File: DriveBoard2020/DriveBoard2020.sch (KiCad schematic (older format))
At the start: 78 parts, among them SW0 SW_SPST, SW1 SW_Push, SW2 SW_Push, SW3 SW_Push, SW4 SW_Push, SW5 SW_Push, SW6 SW_Push, SW7 SW_Push, SW8 SW_Push, SW9 SW_Push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

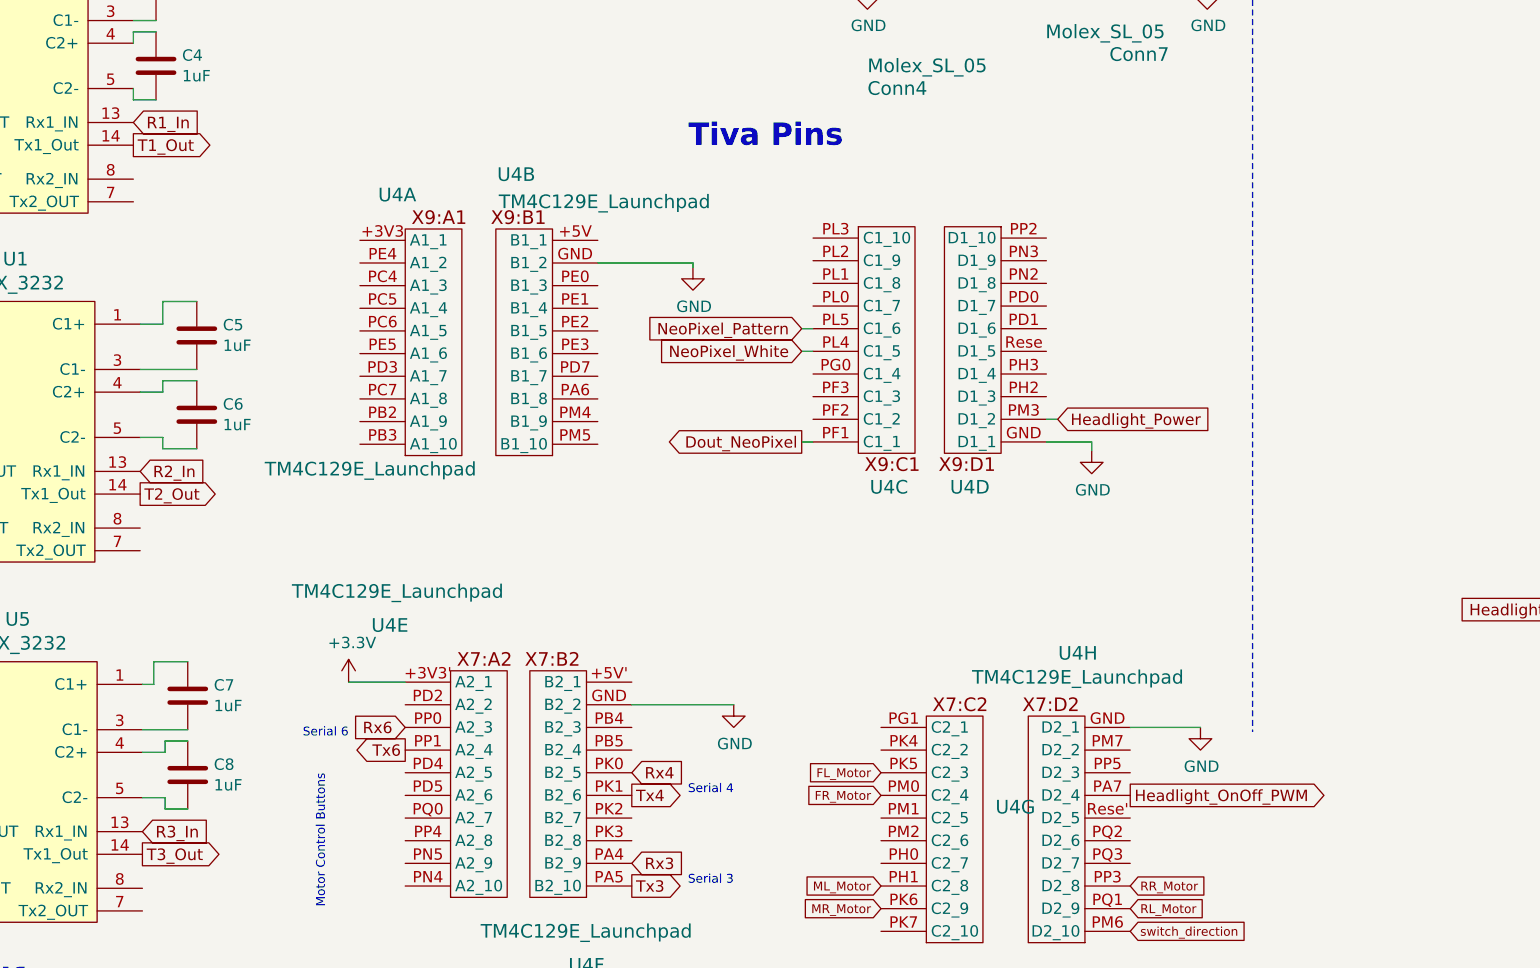
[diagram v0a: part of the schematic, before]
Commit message: finished placing components on layout
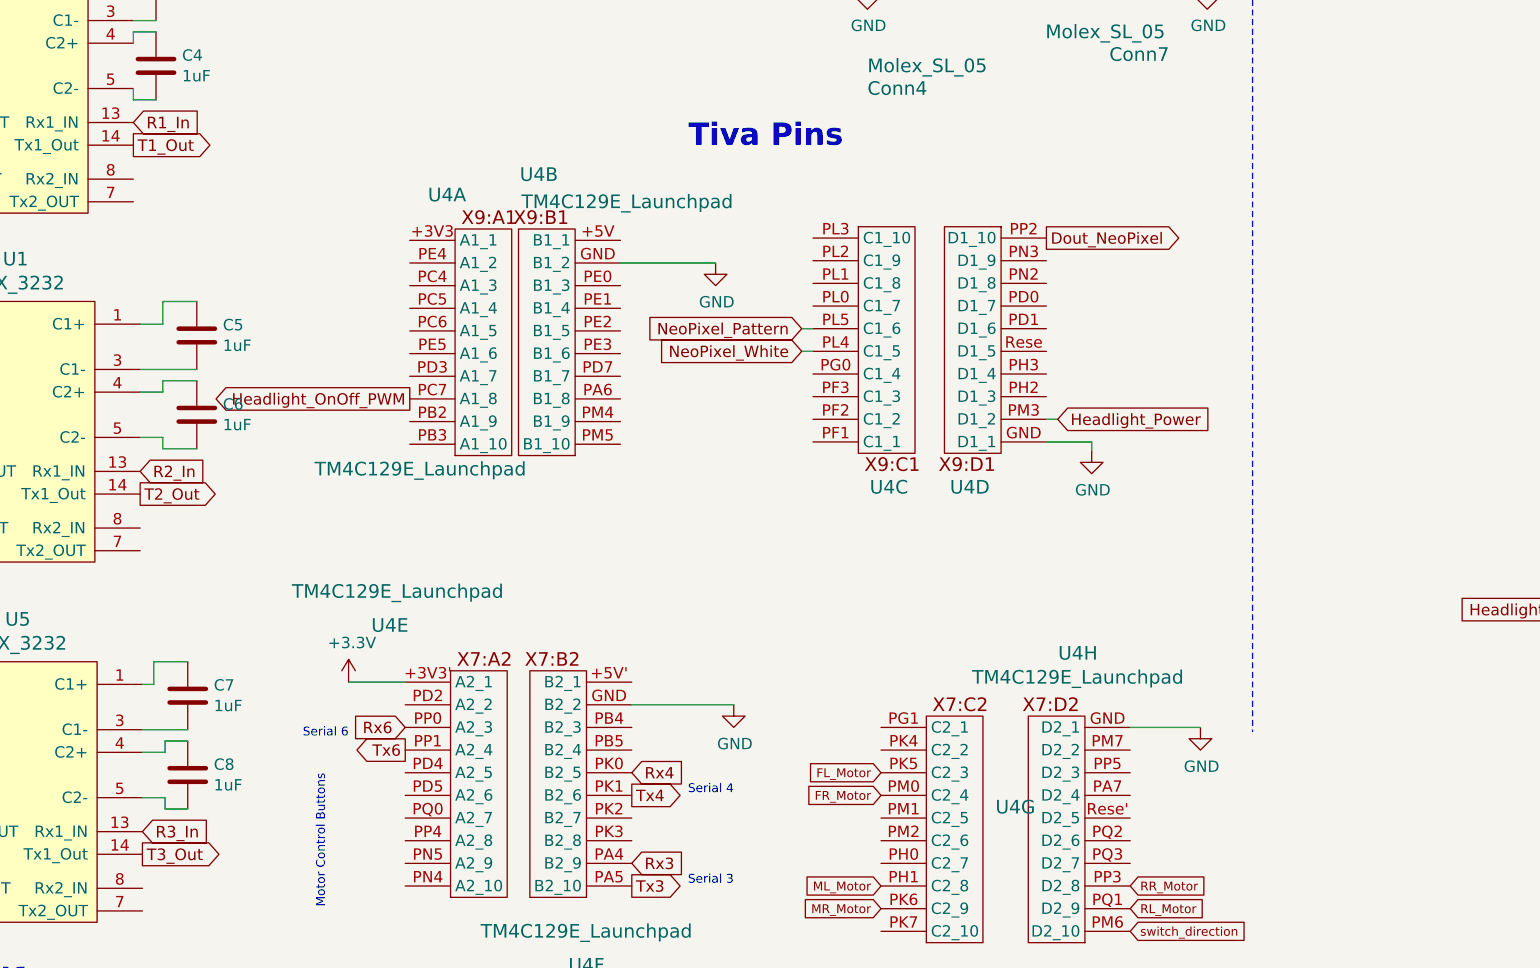
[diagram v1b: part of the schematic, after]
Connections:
- net Dout_NeoPixel: now also U4.PP2 (D1_10); no longer U4.PF1 (C1_1)
- net Headlight_OnOff_PWM: now also U4.PC7 (A1_8); no longer U4.PA7 (D2_4)
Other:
- moved on the sheet: U4A, U4B
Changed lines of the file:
@@
 	1    0    0    1
 $EndComp
-Text GLabel 4980 5260 0    50   Output ~ 0
+Text GLabel 6060 4360 2    50   Output ~ 0
 Dout_NeoPixel
 $Comp
@@
 Wire Wire Line
 	9800 6000 10250 6000
-Wire Wire Line
-	5030 5260 4980 5260
 $Comp
 L power:+5VA #PWR0152
@@
 F 3 "" H 9300 4050 50  0001 C CNN
 	1    9300 4050
-	1    0    0    -1
-$EndComp
-$Comp
-L Device:R R19
-U 1 1 5C7B69E8
-P 9750 4250
-F 0 "R19" H 9820 4296 50  0000 L CNN
-F 1 "500" V 9750 4175 50  0000 L CNN
-F 2 "Resistor_SMD:R_0603_1608Metric_Pad1.05x0.95mm_HandSolder" V 9680 4250 50  0001 C CNN
-F 3 "~" H 9750 4250 50  0001 C CNN
-	1    9750 4250
-	1    0    0    -1
-$EndComp
-$Comp
-L power:GND #PWR0153
-U 1 1 5C7B69EF
-P 9750 4800
-F 0 "#PWR0153" H 9750 4550 50  0001 C CNN
-F 1 "GND" H 9755 4627 50  0000 C CNN
-F 2 "" H 9750 4800 50  0001 C CNN
-F 3 "" H 9750 4800 50  0001 C CNN
-	1    9750 4800
-	1    0    0    -1
-$EndComp
-$Comp
-L Device:LED D16
-U 1 1 5C7B69F5
-P 9750 4600
-F 0 "D16" V 9788 4483 50  0000 R CNN
-F 1 "G_LED" V 9697 4483 50  0000 R CNN
-F 2 "LED_SMD:LED_0603_1608Metric_Pad1.05x0.95mm_HandSolder" H 9750 4600 50  0001 C CNN
-F 3 "~" H 9750 4600 50  0001 C CNN
-	1    9750 4600
-	0    -1   -1   0
-$EndComp
-Wire Wire Line
-	9750 4400 9750 4450
-Wire Wire Line
-	9750 4100 9750 4050
-Wire Wire Line
-	9750 4750 9750 4800
-$Comp
-L power:+5VL #PWR0154
-U 1 1 5C7BB2F1
-P 9750 4050
-F 0 "#PWR0154" H 9750 3900 50  0001 C CNN
-F 1 "+5VL" H 9765 4223 50  0000 C CNN
-F 2 "" H 9750 4050 50  0001 C CNN
-F 3 "" H 9750 4050 50  0001 C CNN
-	1    9750 4050
 	1    0    0    -1
 $EndComp
@@
 L MRDT_Shields:TM4C129E_Launchpad U4
 U 1 1 5DE8D46B
-P 3230 5320
-F 0 "U4" H 3110 6470 60  0000 L CNN
-F 1 "TM4C129E_Launchpad" H 2610 5260 60  0000 L CNN
-F 2 "MRDT_Shields:TM4C129E_Launchpad_FULL_THT_BOTTOM" H 3230 5320 60  0001 C CNN
-F 3 "" H 3230 5320 60  0001 C CNN
-	1    3230 5320
+P 3450 5320
+F 0 "U4" H 3330 6470 60  0000 L CNN
+F 1 "TM4C129E_Launchpad" H 2830 5260 60  0000 L CNN
+F 2 "MRDT_Shields:TM4C129E_Launchpad_FULL_THT_BOTTOM" H 3450 5320 60  0001 C CNN
+F 3 "" H 3450 5320 60  0001 C CNN
+	1    3450 5320
 	1    0    0    -1
 $EndComp
@@
 L MRDT_Shields:TM4C129E_Launchpad U4
 U 2 1 5DE90FB1
-P 3880 5320
-F 0 "U4" H 4040 6560 60  0000 C CNN
-F 1 "TM4C129E_Launchpad" H 3650 6440 60  0000 C CNN
-F 2 "MRDT_Shields:TM4C129E_Launchpad_FULL_THT_BOTTOM" H 3880 5320 60  0001 C CNN
-F 3 "" H 3880 5320 60  0001 C CNN
-	2    3880 5320
+P 3980 5320
+F 0 "U4" H 4140 6560 60  0000 C CNN
+F 1 "TM4C129E_Launchpad" H 3750 6440 60  0000 C CNN
+F 2 "MRDT_Shields:TM4C129E_Launchpad_FULL_THT_BOTTOM" H 3980 5320 60  0001 C CNN
+F 3 "" H 3980 5320 60  0001 C CNN
+	2    3980 5320
 	-1   0    0    -1
 $EndComp
@@
 	-1   0    0    -1
 $EndComp
-Text GLabel 6430 6820 2    50   Output ~ 0
+Text GLabel 3250 5070 0    50   Output ~ 0
 Headlight_OnOff_PWM
 Wire Notes Line style solid
@@
 Wire Wire Line
 	6260 5260 6060 5260
-Wire Wire Line
-	4500 4470 4500 4490
 $Comp
 L power:GND #PWR0146
 U 1 1 5E44A8A8
-P 4500 4490
-F 0 "#PWR0146" H 4500 4240 50  0001 C CNN
-F 1 "GND" H 4505 4317 50  0000 C CNN
-F 2 "" H 4500 4490 50  0001 C CNN
-F 3 "" H 4500 4490 50  0001 C CNN
-	1    4500 4490
-	1    0    0    -1
-$EndComp
-Wire Wire Line
-	4080 4470 4500 4470
+P 4600 4470
+F 0 "#PWR0146" H 4600 4220 50  0001 C CNN
+F 1 "GND" H 4605 4297 50  0000 C CNN
+F 2 "" H 4600 4470 50  0001 C CNN
+F 3 "" H 4600 4470 50  0001 C CNN
+	1    4600 4470
+	1    0    0    -1
+$EndComp
 $Comp
 L power:GND #PWR0150
@@
 	1    0    0    -1
 $EndComp
+Wire Wire Line
+	4180 4470 4600 4470
+$Comp
+L power:+5VL #PWR0154
+U 1 1 5C7BB2F1
+P 9750 4050
+F 0 "#PWR0154" H 9750 3900 50  0001 C CNN
+F 1 "+5VL" H 9765 4223 50  0000 C CNN
+F 2 "" H 9750 4050 50  0001 C CNN
+F 3 "" H 9750 4050 50  0001 C CNN
+	1    9750 4050
+	1    0    0    -1
+$EndComp
+Wire Wire Line
+	9750 4750 9750 4800
+Wire Wire Line
+	9750 4100 9750 4050
+Wire Wire Line
+	9750 4400 9750 4450
+$Comp
+L Device:LED D16
+U 1 1 5C7B69F5
+P 9750 4600
+F 0 "D16" V 9788 4483 50  0000 R CNN
+F 1 "G_LED" V 9697 4483 50  0000 R CNN
+F 2 "LED_SMD:LED_0603_1608Metric_Pad1.05x0.95mm_HandSolder" H 9750 4600 50  0001 C CNN
+F 3 "~" H 9750 4600 50  0001 C CNN
+	1    9750 4600
+	0    -1   -1   0
+$EndComp
+$Comp
+L power:GND #PWR0153
+U 1 1 5C7B69EF
+P 9750 4800
+F 0 "#PWR0153" H 9750 4550 50  0001 C CNN
+F 1 "GND" H 9755 4627 50  0000 C CNN
+F 2 "" H 9750 4800 50  0001 C CNN
+F 3 "" H 9750 4800 50  0001 C CNN
+	1    9750 4800
+	1    0    0    -1
+$EndComp
+$Comp
+L Device:R R19
+U 1 1 5C7B69E8
+P 9750 4250
+F 0 "R19" H 9820 4296 50  0000 L CNN
+F 1 "500" V 9750 4175 50  0000 L CNN
+F 2 "Resistor_SMD:R_0603_1608Metric_Pad1.05x0.95mm_HandSolder" V 9680 4250 50  0001 C CNN
+F 3 "~" H 9750 4250 50  0001 C CNN
+	1    9750 4250
+	1    0    0    -1
+$EndComp

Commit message: traces to layout
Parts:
- removed D10, D12, D14: LED, LED_SMD:LED_0603_1608Metric_Pad1.05x0.95mm_HandSolder, symbol Device:LED
- removed R10, R12, R14: 500, Resistor_SMD:R_0603_1608Metric_Pad1.05x0.95mm_HandSolder, symbol Device:R
- removed SW2, SW4, SW6: SW_Push, Button_Switch_SMD:SW_SPST_TL3305A, symbol Switch:SW_Push
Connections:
- net +5V: now also R19.1
- net +5VL: no longer R19.1
- net Headlight_Power: now also U4.PM5 (B1_10); no longer U4.PM3 (D1_2)
- net NeoPixel_Pattern: now also U4.PM4 (B1_9); no longer U4.PL5 (C1_6)
- net NeoPixel_White: now also U4.PB3 (A1_10); no longer U4.PL4 (C1_5)
- net Front_Motor: now reaches U4.PK4 (C2_2)
- net Front_Motor: now also R9.2, SW1.2
- net Middle_Motor: now reaches U4.PM1 (C2_5)
- net Middle_Motor: now also R11.2, SW3.2
- removed net FL_Motor: R9.2, SW1.2, U4.PK5 (C2_3)
- net FR_Motor: no longer names the net of U4.PM0 (C2_4)
- removed net ML_Motor: R11.2, SW3.2, U4.PH1 (C2_8)
- net MR_Motor: no longer names the net of U4.PK6 (C2_9)
- net RL_Motor renamed Rear_Motor
- net Rear_Motor: now also U4.PH1 (C2_8); no longer U4.PQ1 (D2_9)
- net RR_Motor: no longer names the net of U4.PP3 (D2_8)
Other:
- note removed: "Motor Control Buttons"
- moved on the sheet: U4A, U4B, U4G, U4H

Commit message: cleaned up schematic some
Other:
- note removed: "Lighting"
- moved on the sheet: C1, C10, C2, C3, C4, C5, C6, C7, C8, C9, Conn10, Conn11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
